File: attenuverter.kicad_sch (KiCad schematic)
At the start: 48 parts

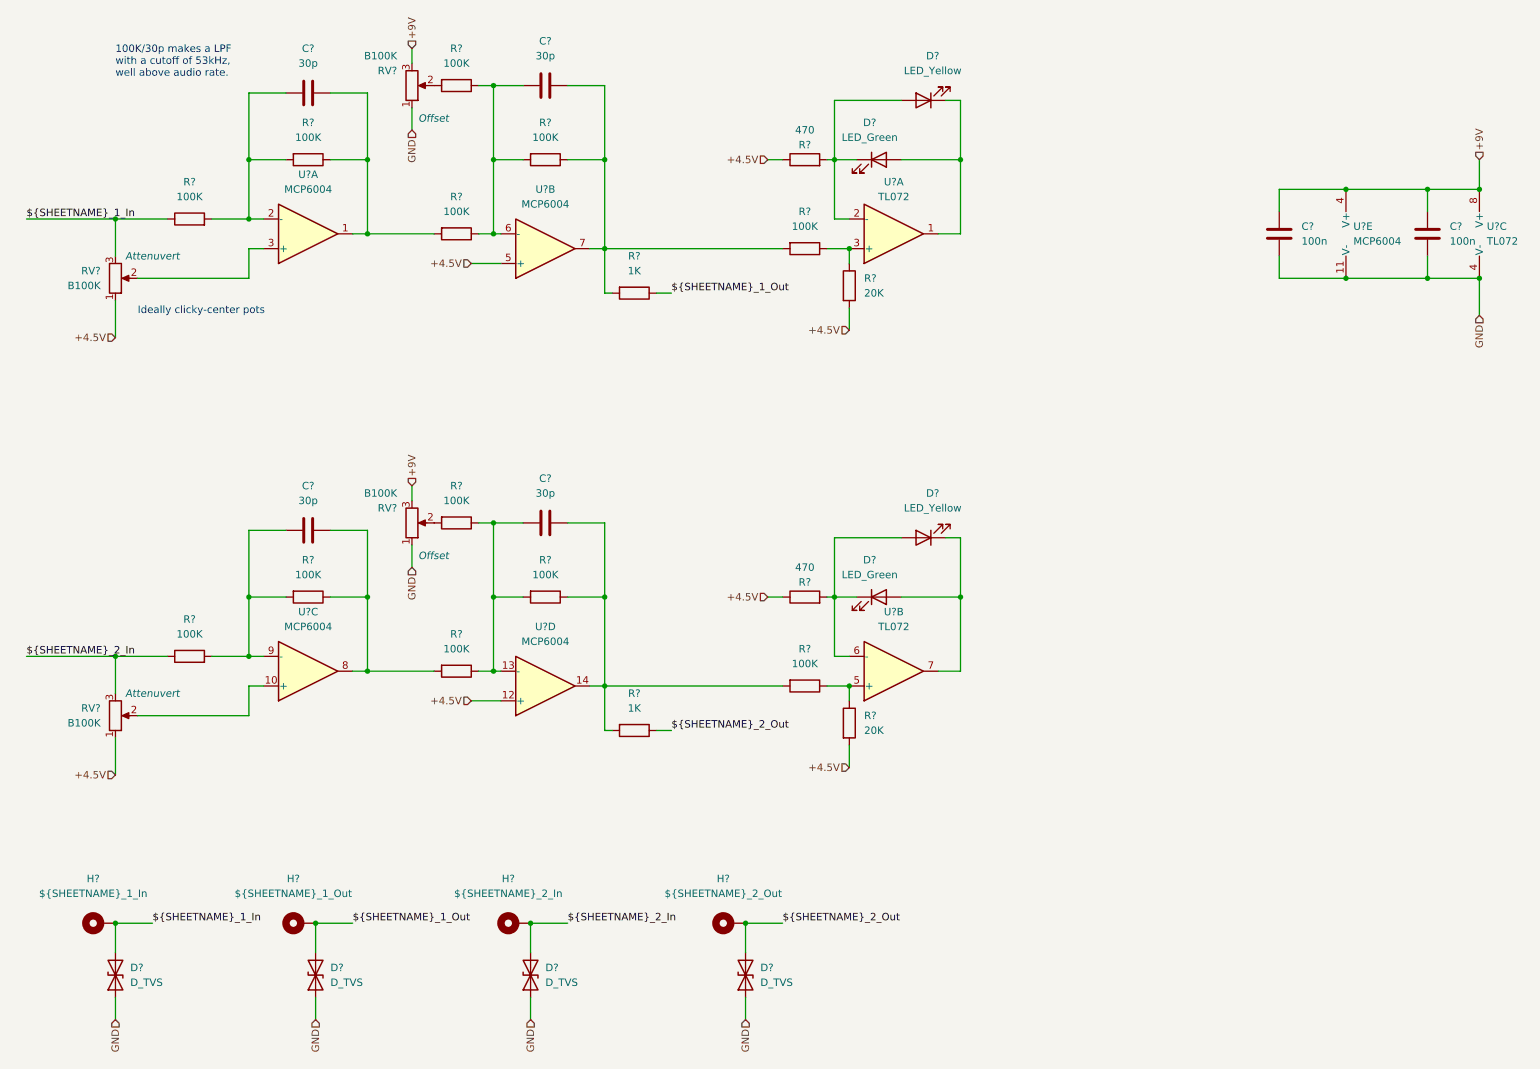
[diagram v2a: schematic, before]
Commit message: Attenuverters laid out
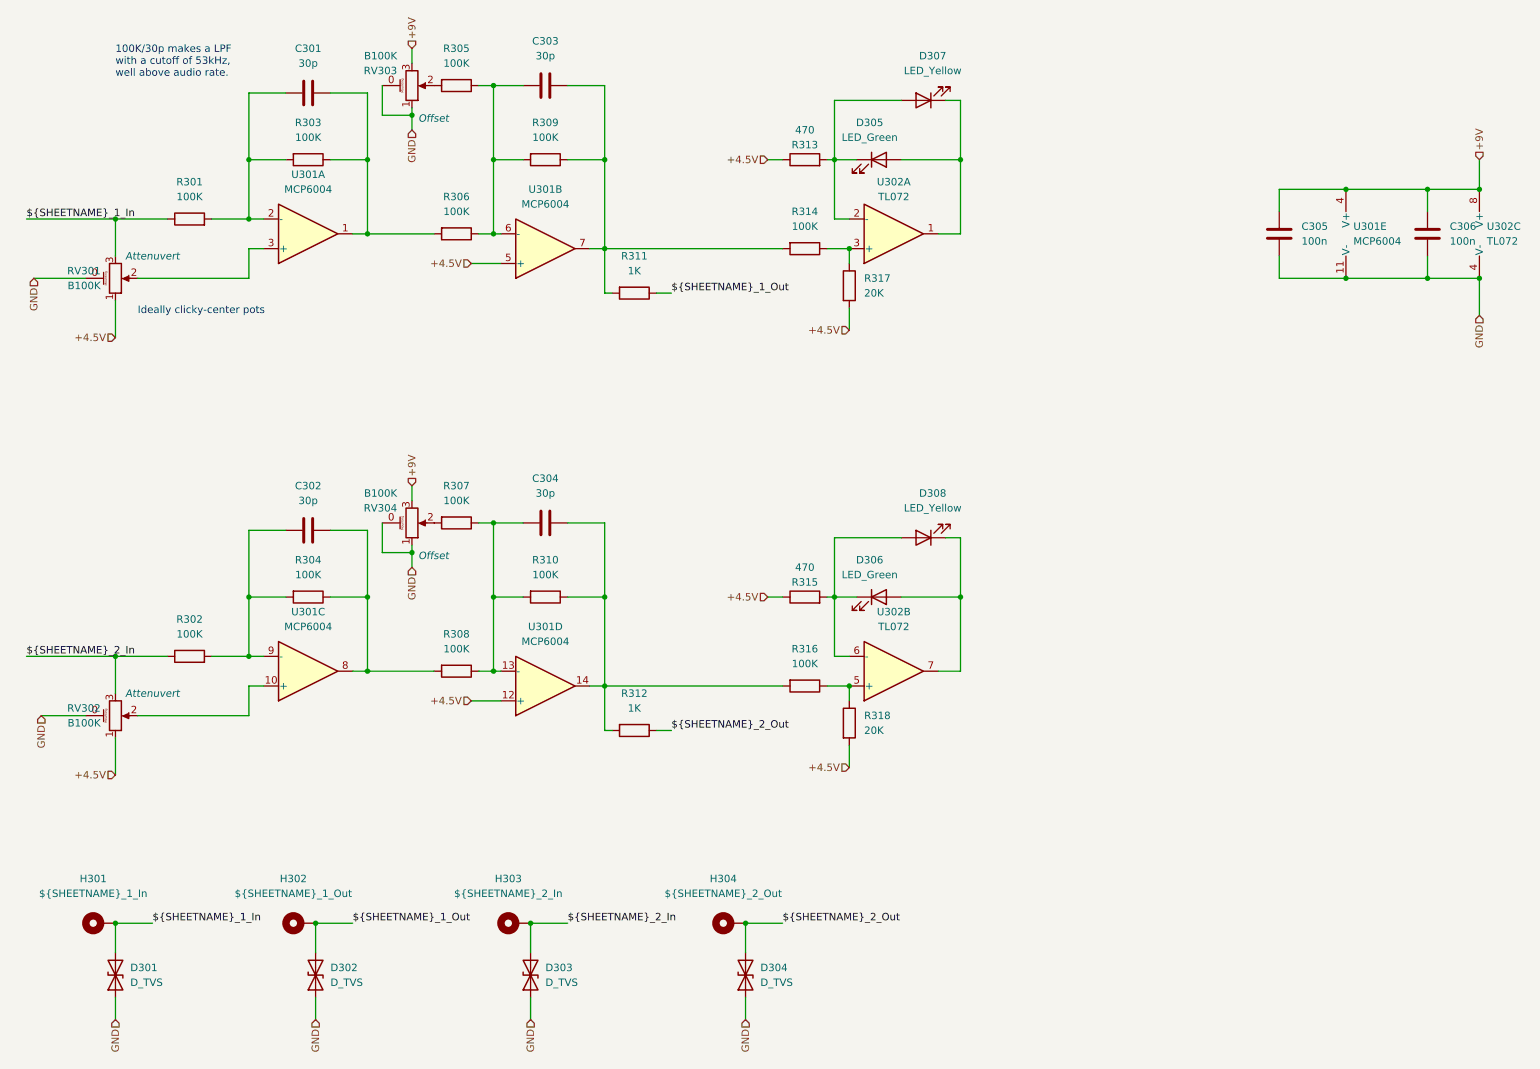
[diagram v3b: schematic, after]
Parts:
- C301, C302, C303, C304, C305, C306: renamed from C?; footprint (none) -> Capacitor_SMD:C_0603_1608Metric_Pad1.08x0.95mm_HandSolder
- D301, D302, D303, D304: renamed from D?; footprint (none) -> Diode_SMD:D_SOD-323_HandSoldering
- D305, D306, D307, D308: renamed from D?; footprint (none) -> LED_THT:LED_D3.0mm
- H301, H302, H303, H304: renamed from H?; footprint (none) -> MountingHole:MountingHole_4.3mm_M4_Pad_TopBottom
- R301, R302, R303, R304, R305, R306, R307, R308, R309, R310, R311, R312, R313, R314, R315, R316, R317, R318: renamed from R?; footprint (none) -> Resistor_SMD:R_0603_1608Metric_Pad0.98x0.95mm_HandSolder
- RV301, RV302, RV303, RV304: renamed from RV?; footprint (none) -> R0904NB10KL-25KQ:V2_TRIM_R0904NB10KL-25KQ-; symbol Device:R_Potentiometer -> R0904NB10KL-25KQ:R_Potentiometer_Shield
- U301: renamed from U?; footprint (none) -> Package_SO:TSSOP-14_4.4x5mm_P0.65mm
- U302: renamed from U?; footprint (none) -> Package_SO:SOIC-8_3.9x4.9mm_P1.27mm
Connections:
- net GND: now also RV301.0 (ShieldPin), RV302.0 (ShieldPin), RV303.0 (ShieldPin), RV304.0 (ShieldPin)

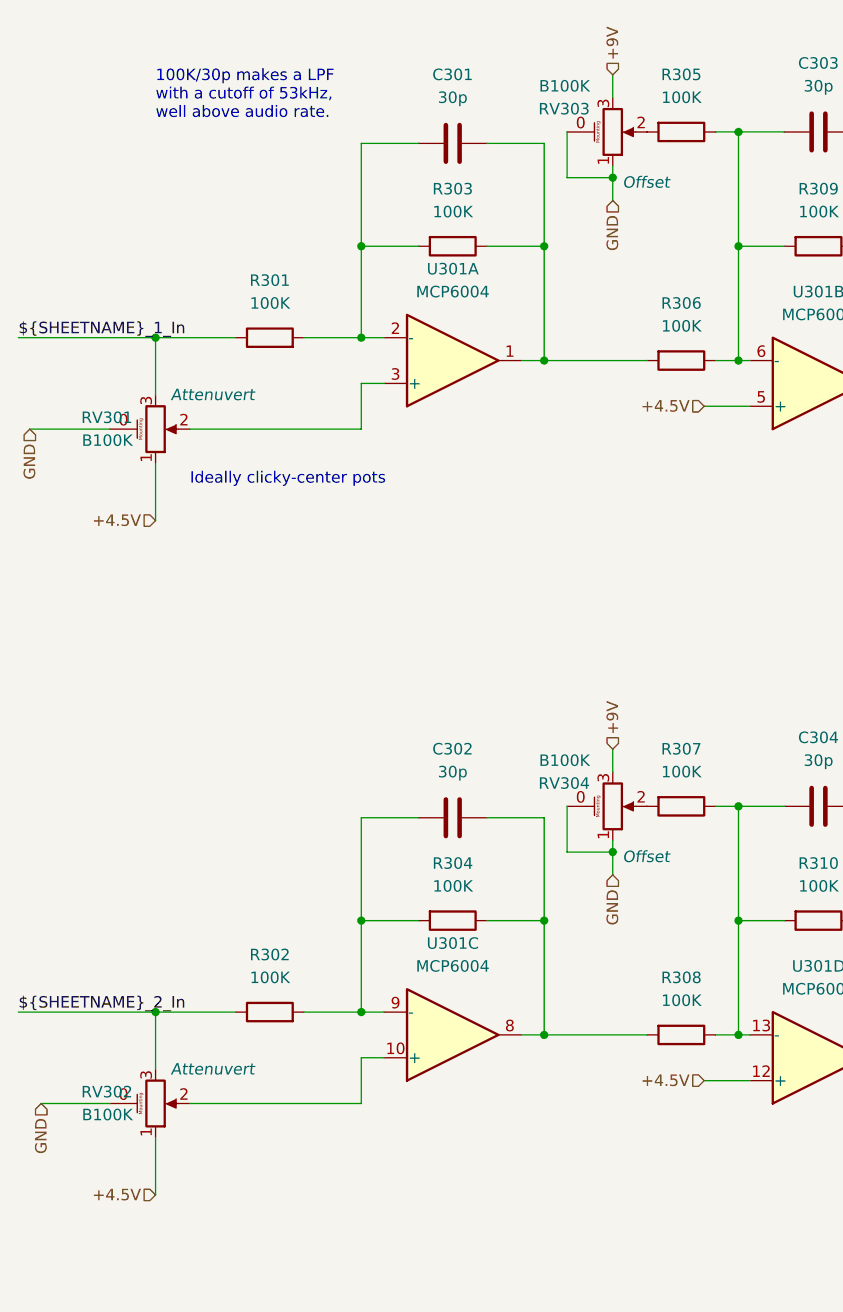
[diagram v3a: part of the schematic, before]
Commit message: Fix attenuverter pots + more design
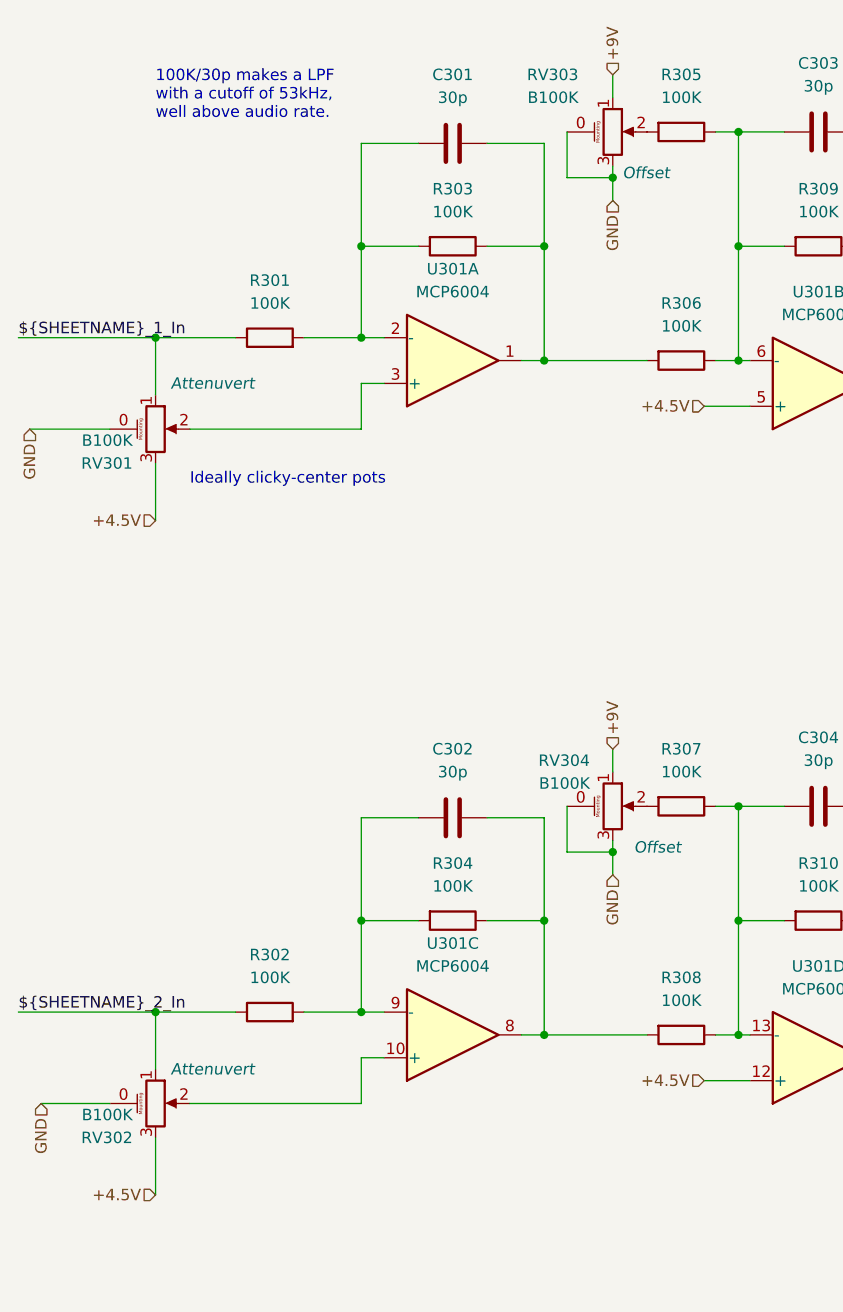
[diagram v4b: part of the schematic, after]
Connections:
- net ${SHEETNAME}_1_In: now also RV301.1; no longer RV301.3
- net ${SHEETNAME}_2_In: now also RV302.1; no longer RV302.3
- net +4.5V: now also RV301.3, RV302.3; no longer RV301.1, RV302.1
- net +9V: now also RV303.1, RV304.1; no longer RV303.3, RV304.3
- net GND: now also RV303.3, RV304.3; no longer RV303.1, RV304.1
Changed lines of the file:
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@@
     (pin "2")
   )
-  (symbol (lib_id "R0904NB10KL-25KQ:R_Potentiometer_Shield") (at 83.82 26.67 0) (mirror x) (unit 1)
+  (symbol (lib_id "R0904NB10KL-25KQ:R_Potentiometer_Shield") (at 83.82 26.67 0) (unit 1)
     (in_bom yes) (on_board yes)
-    (property "Reference" "RV303" (id 0) (at 81.28 24.13 0)
-      (effects (font (size 1.27 1.27)) (justify right))
-    )
-    (property "Value" "B100K" (id 1) (at 81.28 21.59 0)
+    (property "Reference" "RV303" (id 0) (at 80.01 20.32 0)
+      (effects (font (size 1.27 1.27)) (justify right))
+    )
+    (property "Value" "B100K" (id 1) (at 80.01 22.86 0)
       (effects (font (size 1.27 1.27)) (justify right))
     )
@@
       (effects (font (size 1.27 1.27)) hide)
     )
-    (property "Role" "Offset" (id 4) (at 90.17 33.02 0)
+    (property "Role" "Offset" (id 4) (at 90.17 30.48 0)
       (effects (font (size 1.27 1.27) italic) (justify right top))
     )
@@
     (pin "2")
   )
-  (symbol (lib_id "R0904NB10KL-25KQ:R_Potentiometer_Shield") (at 33.02 59.69 0) (mirror x) (unit 1)
+  (symbol (lib_id "R0904NB10KL-25KQ:R_Potentiometer_Shield") (at 33.02 59.69 0) (unit 1)
     (in_bom yes) (on_board yes)
-    (property "Reference" "RV301" (id 0) (at 30.48 58.4199 0)
-      (effects (font (size 1.27 1.27)) (justify right))
-    )
-    (property "Value" "B100K" (id 1) (at 30.48 60.9599 0)
+    (property "Reference" "RV301" (id 0) (at 30.48 63.5 0)
+      (effects (font (size 1.27 1.27)) (justify right))
+    )
+    (property "Value" "B100K" (id 1) (at 30.48 60.96 0)
       (effects (font (size 1.27 1.27)) (justify right))
     )
@@
       (effects (font (size 1.27 1.27)) hide)
     )
-    (property "Role" "Attenuvert" (id 4) (at 39.37 55.88 0)
+    (property "Role" "Attenuvert" (id 4) (at 39.37 54.61 0)
       (effects (font (size 1.27 1.27) italic))
     )
@@
     (pin "2")
   )
-  (symbol (lib_id "R0904NB10KL-25KQ:R_Potentiometer_Shield") (at 83.82 101.6 0) (mirror x) (unit 1)
+  (symbol (lib_id "R0904NB10KL-25KQ:R_Potentiometer_Shield") (at 83.82 101.6 0) (unit 1)
     (in_bom yes) (on_board yes)
-    (property "Reference" "RV304" (id 0) (at 81.28 99.06 0)
-      (effects (font (size 1.27 1.27)) (justify right))
-    )
-    (property "Value" "B100K" (id 1) (at 81.28 96.52 0)
+    (property "Reference" "RV304" (id 0) (at 81.28 96.52 0)
+      (effects (font (size 1.27 1.27)) (justify right))
+    )
+    (property "Value" "B100K" (id 1) (at 81.28 99.06 0)
       (effects (font (size 1.27 1.27)) (justify right))
     )
@@
       (effects (font (size 1.27 1.27)) hide)
     )
-    (property "Role" "Offset" (id 4) (at 90.17 107.95 0)
+    (property "Role" "Offset" (id 4) (at 91.44 105.41 0)
       (effects (font (size 1.27 1.27) italic) (justify right top))
     )
@@
     (pin "1")
   )
-  (symbol (lib_id "R0904NB10KL-25KQ:R_Potentiometer_Shield") (at 33.02 134.62 0) (mirror x) (unit 1)
+  (symbol (lib_id "R0904NB10KL-25KQ:R_Potentiometer_Shield") (at 33.02 134.62 0) (unit 1)
     (in_bom yes) (on_board yes)
-    (property "Reference" "RV302" (id 0) (at 30.48 133.3499 0)
-      (effects (font (size 1.27 1.27)) (justify right))
-    )
-    (property "Value" "B100K" (id 1) (at 30.48 135.8899 0)
-      (effects (font (size 1.27 1.27)) (justify right))
-    )
+    (property "Reference" "RV302" (id 0) (at 30.48 138.43 0)
+      (effects (font (size 1.27 1.27)) (justify right))
+    )
+    (property "Value" "B100K" (id 1) (at 30.48 135.89 0)
+      (effects (font (size 1.27 1.27)) (justify right))
+    )

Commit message: VCF schem combed
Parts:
- C301, C302, C303, C304: value 30p -> 10p
- U301: footprint Package_SO:TSSOP-14_4.4x5mm_P0.65mm -> Package_SO:SOIC-14_3.9x8.7mm_P1.27mm
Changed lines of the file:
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@@
     (in_bom yes) (on_board yes) (fields_autoplaced)
     (property "Reference" "C304" (id 0) (at 106.68 93.98 90))
-    (property "Value" "30p" (id 1) (at 106.68 96.52 90))
+    (property "Value" "10p" (id 1) (at 106.68 96.52 90))
     (property "Footprint" "Capacitor_SMD:C_0603_1608Metric_Pad1.08x0.95mm_HandSolder" (id 2) (at 110.49 100.6348 0)
       (effects (font (size 1.27 1.27)) hide)
@@
     (in_bom yes) (on_board yes) (fields_autoplaced)
     (property "Reference" "C301" (id 0) (at 66.04 20.32 90))
-    (property "Value" "30p" (id 1) (at 66.04 22.86 90))
+    (property "Value" "10p" (id 1) (at 66.04 22.86 90))
     (property "Footprint" "Capacitor_SMD:C_0603_1608Metric_Pad1.08x0.95mm_HandSolder" (id 2) (at 69.85 26.9748 0)
       (effects (font (size 1.27 1.27)) hide)
@@
     (in_bom yes) (on_board yes) (fields_autoplaced)
     (property "Reference" "C303" (id 0) (at 106.68 19.05 90))
-    (property "Value" "30p" (id 1) (at 106.68 21.59 90))
+    (property "Value" "10p" (id 1) (at 106.68 21.59 90))
     (property "Footprint" "Capacitor_SMD:C_0603_1608Metric_Pad1.08x0.95mm_HandSolder" (id 2) (at 110.49 25.7048 0)
       (effects (font (size 1.27 1.27)) hide)
@@
     (property "Reference" "U301" (id 0) (at 106.68 119.38 0))
     (property "Value" "MCP6004" (id 1) (at 106.68 121.92 0))
-    (property "Footprint" "Package_SO:TSSOP-14_4.4x5mm_P0.65mm" (id 2) (at 105.41 132.08 0)
+    (property "Footprint" "Package_SO:SOIC-14_3.9x8.7mm_P1.27mm" (id 2) (at 105.41 132.08 0)
       (effects (font (size 1.27 1.27)) hide)
     )
@@
       (effects (font (size 1.27 1.27)) (justify left))
     )
-    (property "Footprint" "Package_SO:TSSOP-14_4.4x5mm_P0.65mm" (id 2) (at 245.11 49.53 0)
+    (property "Footprint" "Package_SO:SOIC-14_3.9x8.7mm_P1.27mm" (id 2) (at 245.11 49.53 0)
       (effects (font (size 1.27 1.27)) hide)
     )
@@
     (property "Reference" "U301" (id 0) (at 66.04 116.84 0))
     (property "Value" "MCP6004" (id 1) (at 66.04 119.38 0))
-    (property "Footprint" "Package_SO:TSSOP-14_4.4x5mm_P0.65mm" (id 2) (at 64.77 129.54 0)
+    (property "Footprint" "Package_SO:SOIC-14_3.9x8.7mm_P1.27mm" (id 2) (at 64.77 129.54 0)
       (effects (font (size 1.27 1.27)) hide)
     )
@@
     (property "Reference" "U301" (id 0) (at 106.68 44.45 0))
     (property "Value" "MCP6004" (id 1) (at 106.68 46.99 0))
-    (property "Footprint" "Package_SO:TSSOP-14_4.4x5mm_P0.65mm" (id 2) (at 105.41 57.15 0)
+    (property "Footprint" "Package_SO:SOIC-14_3.9x8.7mm_P1.27mm" (id 2) (at 105.41 57.15 0)
       (effects (font (size 1.27 1.27)) hide)
     )
@@
     (in_bom yes) (on_board yes) (fields_autoplaced)
     (property "Reference" "C302" (id 0) (at 66.04 95.25 90))
-    (property "Value" "30p" (id 1) (at 66.04 97.79 90))
+    (property "Value" "10p" (id 1) (at 66.04 97.79 90))
     (property "Footprint" "Capacitor_SMD:C_0603_1608Metric_Pad1.08x0.95mm_HandSolder" (id 2) (at 69.85 101.9048 0)
       (effects (font (size 1.27 1.27)) hide)
@@
     (property "Reference" "U301" (id 0) (at 66.04 41.91 0))
     (property "Value" "MCP6004" (id 1) (at 66.04 44.45 0))
-    (property "Footprint" "Package_SO:TSSOP-14_4.4x5mm_P0.65mm" (id 2) (at 64.77 54.61 0)
-      (effects (font (size 1.27 1.27)) hide)
-    )
+    (property "Footprint" "Package_SO:SOIC-14_3.9x8.7mm_P1.27mm" (id 2) (at 64.77 54.61 0)
+      (effects (font (size 1.27 1.27)) hide)
+    )

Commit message: VCF layout done, vca capture
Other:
- note added: "100K/10p makes a LPF with a cutoff of 160kHz, well above audio rate."
- note added: "Attenuverters"
- note removed: "100K/30p makes a LPF with a cutoff of 53kHz, well above audio rate."
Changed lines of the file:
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@@
     (stroke (width 0) (type default) (color 0 0 0 0))
   )
-  (text "100K/30p makes a LPF\nwith a cutoff of 53kHz,\nwell above audio rate."
+  (text "Attenuverters" (at 15.24 16.51 0)
+    (effects (font (size 1.27 1.27)) (justify left bottom))
+  )
+  (text "100K/10p makes a LPF\nwith a cutoff of 160kHz,\nwell above audio rate."
     (at 33.02 25.4 0)
     (effects (font (size 1.27 1.27)) (justify left bottom))

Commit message: LFO schem capture done / replace r2r opamps
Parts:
- U301: value MCP6004 -> OPA4991
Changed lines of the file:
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@@
     (in_bom yes) (on_board yes) (fields_autoplaced)
     (property "Reference" "U301" (id 0) (at 106.68 119.38 0))
-    (property "Value" "MCP6004" (id 1) (at 106.68 121.92 0))
+    (property "Value" "OPA4991" (id 1) (at 106.68 121.92 0))
     (property "Footprint" "Package_SO:SOIC-14_3.9x8.7mm_P1.27mm" (id 2) (at 105.41 132.08 0)
       (effects (font (size 1.27 1.27)) hide)
@@
       (effects (font (size 1.27 1.27)) (justify left))
     )
-    (property "Value" "MCP6004" (id 1) (at 245.11 53.3399 0)
+    (property "Value" "OPA4991" (id 1) (at 245.11 53.3399 0)
       (effects (font (size 1.27 1.27)) (justify left))
     )
@@
     (in_bom yes) (on_board yes) (fields_autoplaced)
     (property "Reference" "U301" (id 0) (at 66.04 116.84 0))
-    (property "Value" "MCP6004" (id 1) (at 66.04 119.38 0))
+    (property "Value" "OPA4991" (id 1) (at 66.04 119.38 0))
     (property "Footprint" "Package_SO:SOIC-14_3.9x8.7mm_P1.27mm" (id 2) (at 64.77 129.54 0)
       (effects (font (size 1.27 1.27)) hide)
@@
     (in_bom yes) (on_board yes) (fields_autoplaced)
     (property "Reference" "U301" (id 0) (at 106.68 44.45 0))
-    (property "Value" "MCP6004" (id 1) (at 106.68 46.99 0))
+    (property "Value" "OPA4991" (id 1) (at 106.68 46.99 0))
     (property "Footprint" "Package_SO:SOIC-14_3.9x8.7mm_P1.27mm" (id 2) (at 105.41 57.15 0)
       (effects (font (size 1.27 1.27)) hide)
@@
     (in_bom yes) (on_board yes) (fields_autoplaced)
     (property "Reference" "U301" (id 0) (at 66.04 41.91 0))
-    (property "Value" "MCP6004" (id 1) (at 66.04 44.45 0))
+    (property "Value" "OPA4991" (id 1) (at 66.04 44.45 0))
     (property "Footprint" "Package_SO:SOIC-14_3.9x8.7mm_P1.27mm" (id 2) (at 64.77 54.61 0)
       (effects (font (size 1.27 1.27)) hide)
